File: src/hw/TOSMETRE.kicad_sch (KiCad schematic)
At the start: 61 parts, among them J1 Barrel_Jack_Switch, J2 Conn_01x02_Male, J3 Conn_01x08_Male, J4 Conn_Coaxial, J5 Conn_01x05_Male, J6 Conn_01x02_Male, J7 Conn_Coaxial, SW1 SW_DIP_x01, U1 TPS70950DBVT, U2 18F1320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

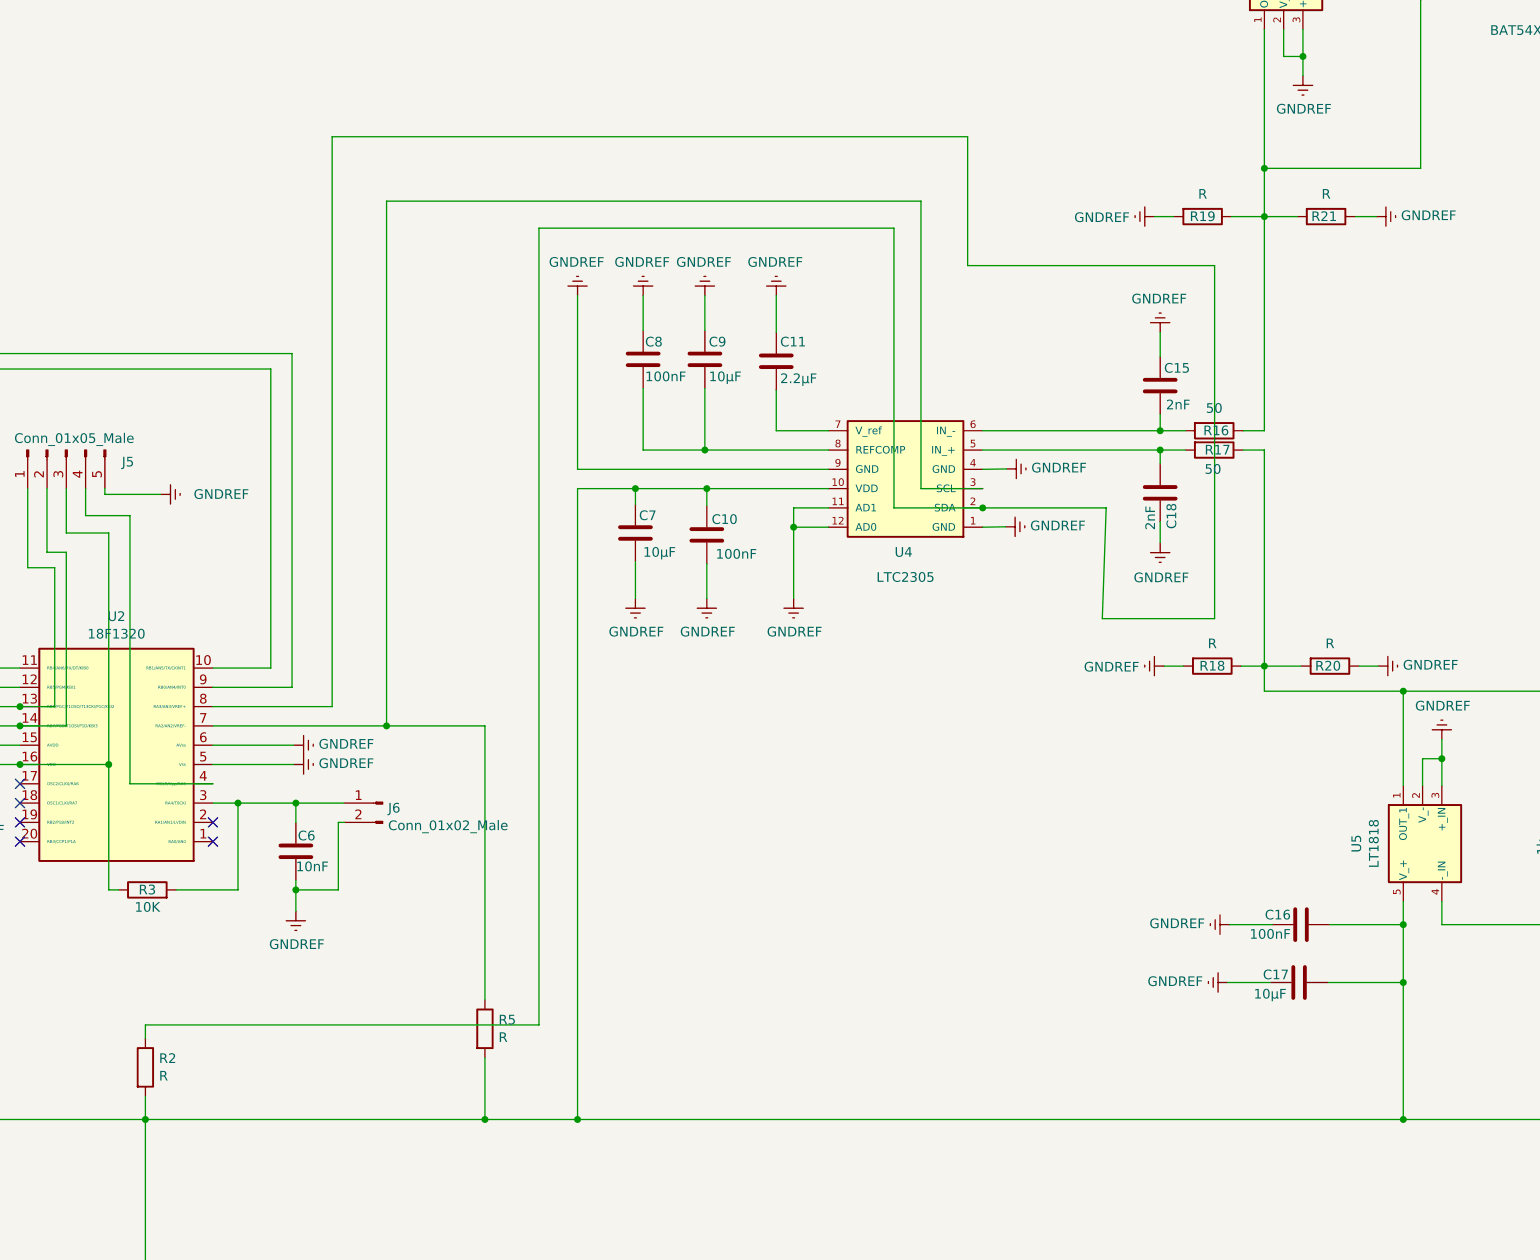
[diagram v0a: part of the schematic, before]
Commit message: #417
si rajout de R1 (à Ohms) plus de piste sous R16 et R17
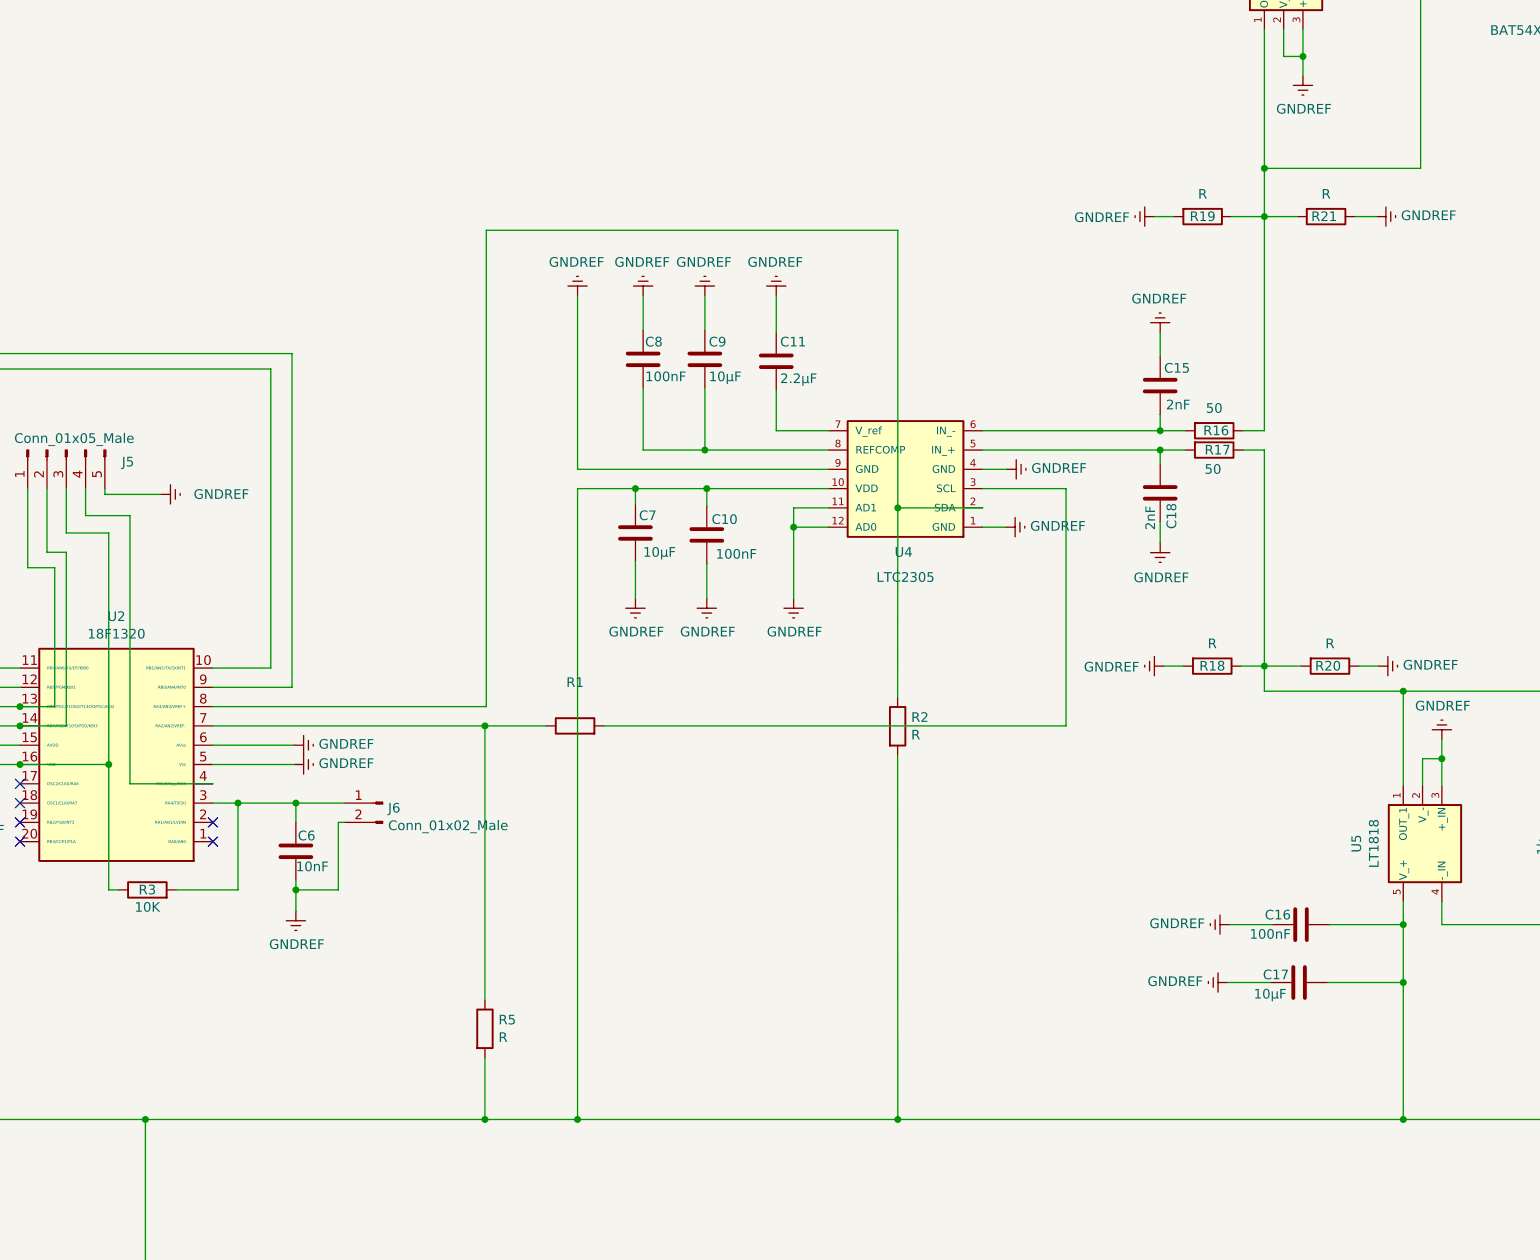
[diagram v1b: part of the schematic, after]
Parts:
- added R1: (no value), symbol Device:R
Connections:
- net at R5.1, U2.7 (RA2/AN2/VREF-): now also R1.1; no longer U4.3 (SCL)
- new net: R1.2, U4.3 (SCL)
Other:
- moved on the sheet: R2
